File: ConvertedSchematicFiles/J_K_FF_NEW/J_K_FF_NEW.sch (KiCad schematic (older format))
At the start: 16 parts, among them U1 74107, U2 74107, U3 74107, U4 74107

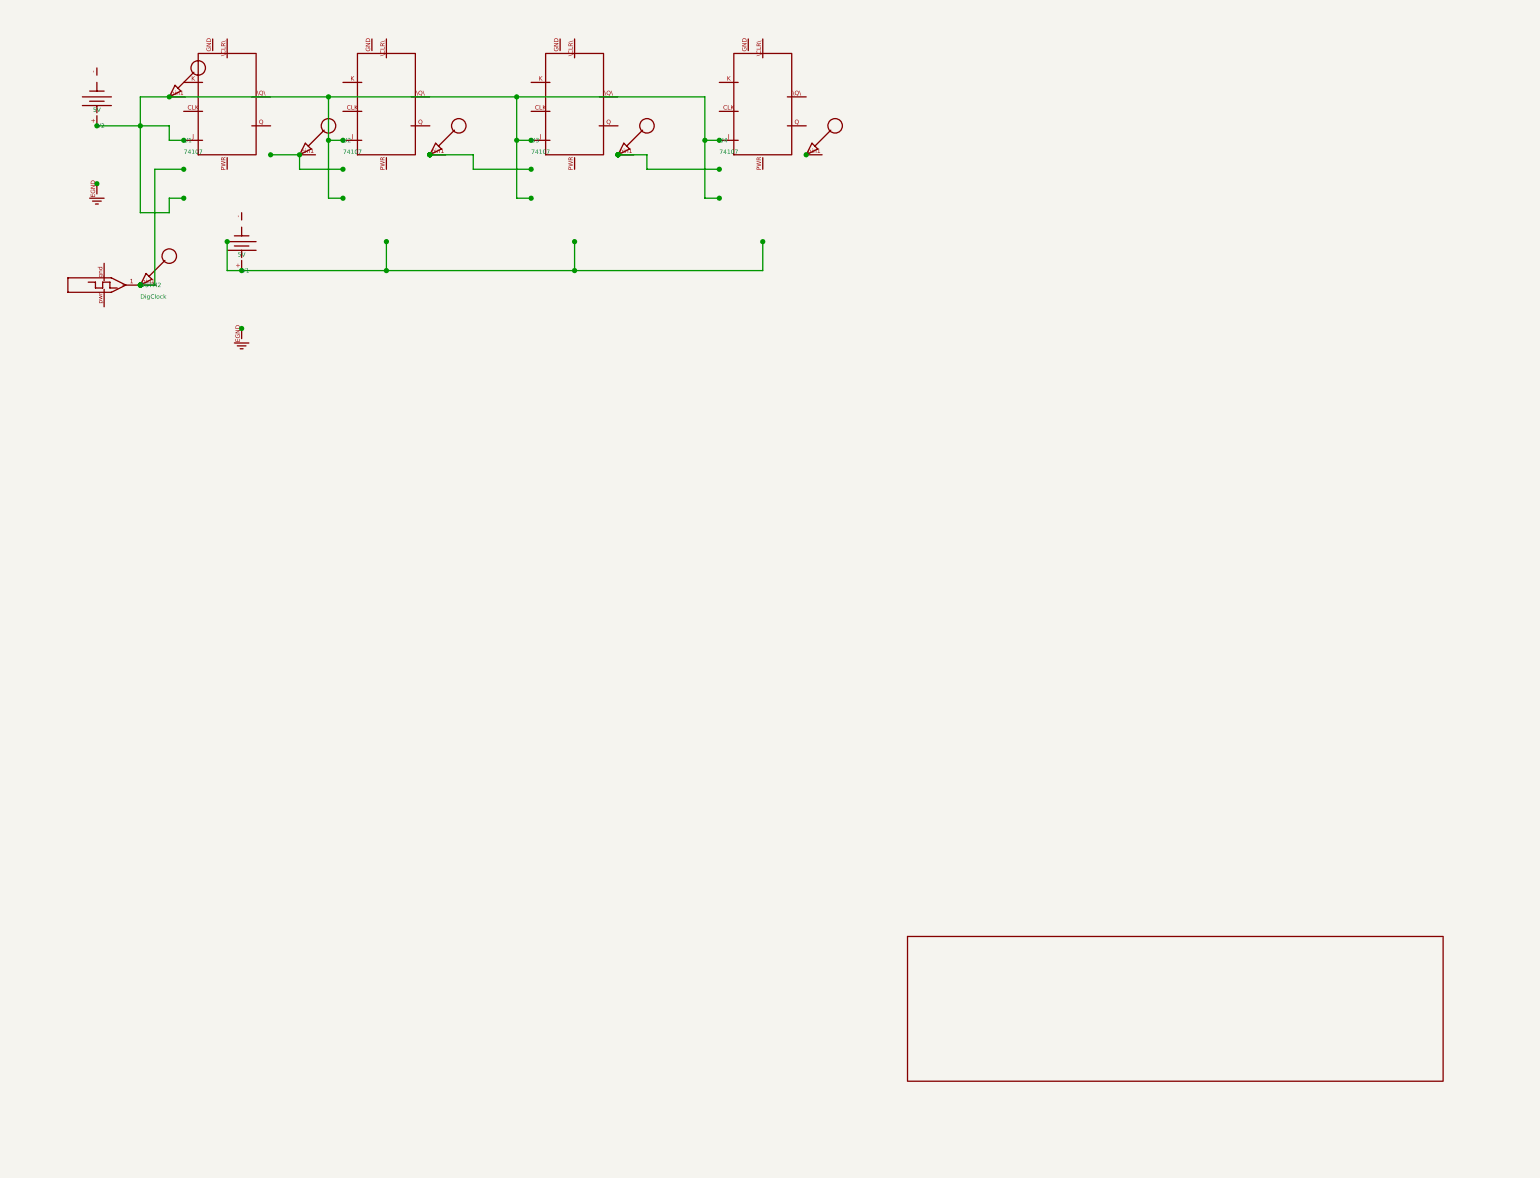
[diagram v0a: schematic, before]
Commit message: Excluded some components. These no longer appear after conversion. When calling shell commands, filenames are in "quotes"
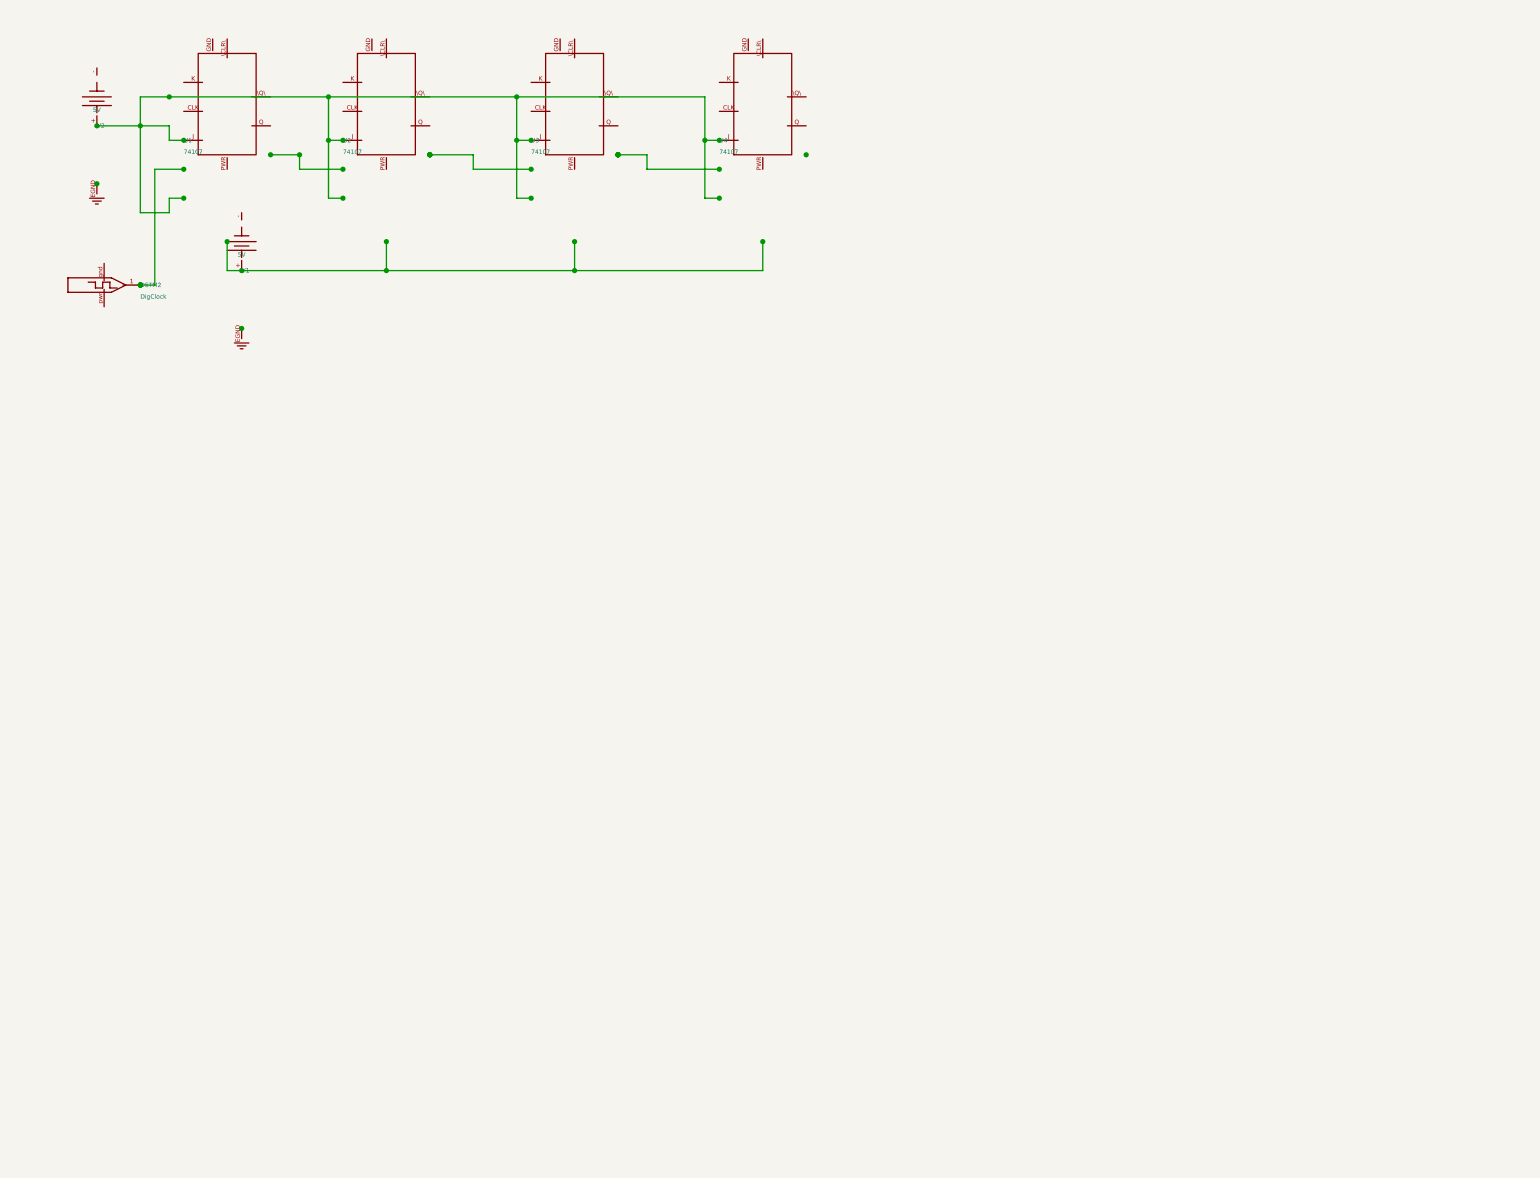
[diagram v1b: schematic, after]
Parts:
- removed nodeMarker (x6): nodeMarker, symbol NODEMARKER_PSPICE
- removed titleblk: titleblk, symbol TITLEBLK_PSPICE
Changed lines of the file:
@@
-	1    0    0    1
-$EndComp
-$Comp
-L TITLEBLK_PSPICE titleblk
-U 1 1 29641421
-P 9700 7200
-F 0 "titleblk" H 19400 14400 30  0001 L CNN
-F 1 "titleblk" H 19400 14480 30  0001 L CNN
-	1    9700 7200
-	1    0    0    1
-$EndComp
-$Comp
-L NODEMARKER_PSPICE nodeMarker
-U 1 1 45202362
-P 1800 800
-F 0 "nodeMarker" H 3600 1600 30  0001 L CNN
-F 1 "nodeMarker" H 3600 1680 30  0001 L CNN
-	1    1800 800
-	1    0    0    1
-$EndComp
-$Comp
-L NODEMARKER_PSPICE nodeMarker
-U 1 1 10490027
-P 700 1700
-F 0 "nodeMarker" H 1400 3400 30  0001 L CNN
-F 1 "nodeMarker" H 1400 3480 30  0001 L CNN
-	1    700 1700
-	1    0    0    1
-$EndComp
-$Comp
-L NODEMARKER_PSPICE nodeMarker
-U 1 1 73368690
-P 900 400
-F 0 "nodeMarker" H 1800 800 30  0001 L CNN
-F 1 "nodeMarker" H 1800 880 30  0001 L CNN
-	1    900 400
-	1    0    0    1
-$EndComp
-$Comp
-L NODEMARKER_PSPICE nodeMarker
-U 1 1 32520059
-P 2700 800
-F 0 "nodeMarker" H 5400 1600 30  0001 L CNN
-F 1 "nodeMarker" H 5400 1680 30  0001 L CNN
-	1    2700 800
-	1    0    0    1
-$EndComp
-$Comp
-L NODEMARKER_PSPICE nodeMarker
-U 1 1 74897763
-P 4000 800
-F 0 "nodeMarker" H 8000 1600 30  0001 L CNN
-F 1 "nodeMarker" H 8000 1680 30  0001 L CNN
-	1    4000 800
-	1    0    0    1
-$EndComp
-$Comp
-L NODEMARKER_PSPICE nodeMarker
-U 1 1 87513926
-P 5300 800
-F 0 "nodeMarker" H 10600 1600 30  0001 L CNN
-F 1 "nodeMarker" H 10600 1680 30  0001 L CNN
-	1    5300 800
 	1    0    0    1
 $EndComp

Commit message: Ports issue fixed. Now annotation for ports is #PWR? function added "itos"
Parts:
- removed EGND (x2): EGND, symbol EGND_PSPICE
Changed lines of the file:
@@
 $EndDescr
 $Comp
-L EGND_PSPICE EGND
+L EGND_PSPICE #PWR1
 U 1 1 14289383
 P 400 1000
-F 0 "EGND" H 800 2000 30  0001 L CNN
+F 0 "#PWR1" H 800 2000 30  0001 L CNN
 F 1 "EGND" H 800 2080 30  0001 L CNN
 	1    400 1000
@@
 $EndComp
 $Comp
-L EGND_PSPICE EGND
+L EGND_PSPICE #PWR2
 U 1 1 46930886
 P 1400 2000
-F 0 "EGND" H 2800 4000 30  0001 L CNN
+F 0 "#PWR2" H 2800 4000 30  0001 L CNN
 F 1 "EGND" H 2800 4080 30  0001 L CNN
 	1    1400 2000

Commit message: Added LICENSE.txt
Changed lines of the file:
@@
 $EndDescr
 $Comp
-L EGND_PSPICE #PWR1
+L GND #PWR1
 U 1 1 14289383
 P 400 1000
@@
 $EndComp
 $Comp
-L EGND_PSPICE #PWR2
+L GND #PWR2
 U 1 1 46930886
 P 1400 2000

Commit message: Orientation fix. Library components are now inverted, with +ve y axis going up. In Schematic files, +ve y axis is downwards. This is how the KiCad libraries are. As a result of the above fixed, the converted GND is now oriented correctly.
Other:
- moved on the sheet: U1, U2, U3, U4, V1, V2
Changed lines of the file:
@@
 F 1 "EGND" H 800 2080 30  0001 L CNN
 	1    400 1000
-	1    0    0    1
+	1    0    0    -1
 $EndComp
 $Comp
@@
 F 1 "EGND" H 2800 4080 30  0001 L CNN
 	1    1400 2000
-	1    0    0    1
+	1    0    0    -1
 $EndComp
 $Comp
@@
 F 1 "74107" H 1000 780 30  0000 L CNN
 	1    1000 700
-	1    0    0    1
+	1    0    0    -1
 $EndComp
 $Comp
@@
 F 1 "DigClock" H 700 1780 30  0000 L CNN
 	1    700 1700
-	1    0    0    1
+	1    0    0    -1
 $EndComp
 $Comp
@@
 F 1 "5V" H 1400 1490 30  0000 C CNN
 	1    1400 1600
-	1    0    0    1
+	1    0    0    -1
 $EndComp
 $Comp
@@
 F 1 "5V" H 400 490 30  0000 C CNN
 	1    400 600
-	1    0    0    1
+	1    0    0    -1
 $EndComp
 $Comp
@@
 F 1 "74107" H 2100 780 30  0000 L CNN
 	1    2100 700
-	1    0    0    1
+	1    0    0    -1
 $EndComp
 $Comp
@@
 F 1 "74107" H 3400 780 30  0000 L CNN
 	1    3400 700
-	1    0    0    1
+	1    0    0    -1
 $EndComp
 $Comp
@@
 F 1 "74107" H 4700 780 30  0000 L CNN
 	1    4700 700
-	1    0    0    1
+	1    0    0    -1
 $EndComp
 Wire Wire Line

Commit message: Removed the use of exec, wrote basename function, made integration with eSim easier.
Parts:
- added nodeMarker (x6): nodeMarker, symbol nodeMarker_PSPICE
- added titleblk: titleblk, symbol titleblk_PSPICE
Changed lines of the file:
@@
-EESchema Schematic File Version 2  date Saturday 17 July 1999 12:21:09 PM IST
+EESchema Schematic File Version 2  date
 LIBS:power
 LIBS:device
@@
 LIBS:contrib
 LIBS:valves
-LIBS:ConvertedSchematicFiles/J_K_FF_NEW-cache
 EELAYER 25  0
 EELAYER END
@@
 Sheet 1 1
 Title ""
-Date "17 Jul 1999"
+Date ""
 Rev ""
 Comp ""
@@
 	1    0    0    -1
 $EndComp
+$Comp
+L titleblk_PSPICE titleblk
+U 1 1 29641421
+P 9700 7200
+F 0 "titleblk" H 19400 14400 30  0001 L CNN
+F 1 "titleblk" H 19400 14480 30  0001 L CNN
+	1    9700 7200
+	1    0    0    -1
+$EndComp
+$Comp
+L nodeMarker_PSPICE nodeMarker
+U 1 1 45202362
+P 1800 800
+F 0 "nodeMarker" H 3600 1600 30  0001 L CNN
+F 1 "nodeMarker" H 3600 1680 30  0001 L CNN
+	1    1800 800
+	1    0    0    -1
+$EndComp
+$Comp
+L nodeMarker_PSPICE nodeMarker
+U 1 1 10490027
+P 700 1700
+F 0 "nodeMarker" H 1400 3400 30  0001 L CNN
+F 1 "nodeMarker" H 1400 3480 30  0001 L CNN
+	1    700 1700
+	1    0    0    -1
+$EndComp
+$Comp
+L nodeMarker_PSPICE nodeMarker
+U 1 1 73368690
+P 900 400
+F 0 "nodeMarker" H 1800 800 30  0001 L CNN
+F 1 "nodeMarker" H 1800 880 30  0001 L CNN
+	1    900 400
+	1    0    0    -1
+$EndComp
+$Comp
+L nodeMarker_PSPICE nodeMarker
+U 1 1 32520059
+P 2700 800
+F 0 "nodeMarker" H 5400 1600 30  0001 L CNN
+F 1 "nodeMarker" H 5400 1680 30  0001 L CNN
+	1    2700 800
+	1    0    0    -1
+$EndComp
+$Comp
+L nodeMarker_PSPICE nodeMarker
+U 1 1 74897763
+P 4000 800
+F 0 "nodeMarker" H 8000 1600 30  0001 L CNN
+F 1 "nodeMarker" H 8000 1680 30  0001 L CNN
+	1    4000 800
+	1    0    0    -1
+$EndComp
+$Comp
+L nodeMarker_PSPICE nodeMarker
+U 1 1 87513926
+P 5300 800
+F 0 "nodeMarker" H 10600 1600 30  0001 L CNN
+F 1 "nodeMarker" H 10600 1680 30  0001 L CNN
+	1    5300 800
+	1    0    0    -1
+$EndComp
